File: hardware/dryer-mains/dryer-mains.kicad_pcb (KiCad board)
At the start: 2 copper layers, 64 x 85 mm, 19 parts, among them K1 SRD-05VDC-SL-C, K2 SRD-05VDC-SL-C, Q1 MMBT2222A, Q2 MMBT2222A

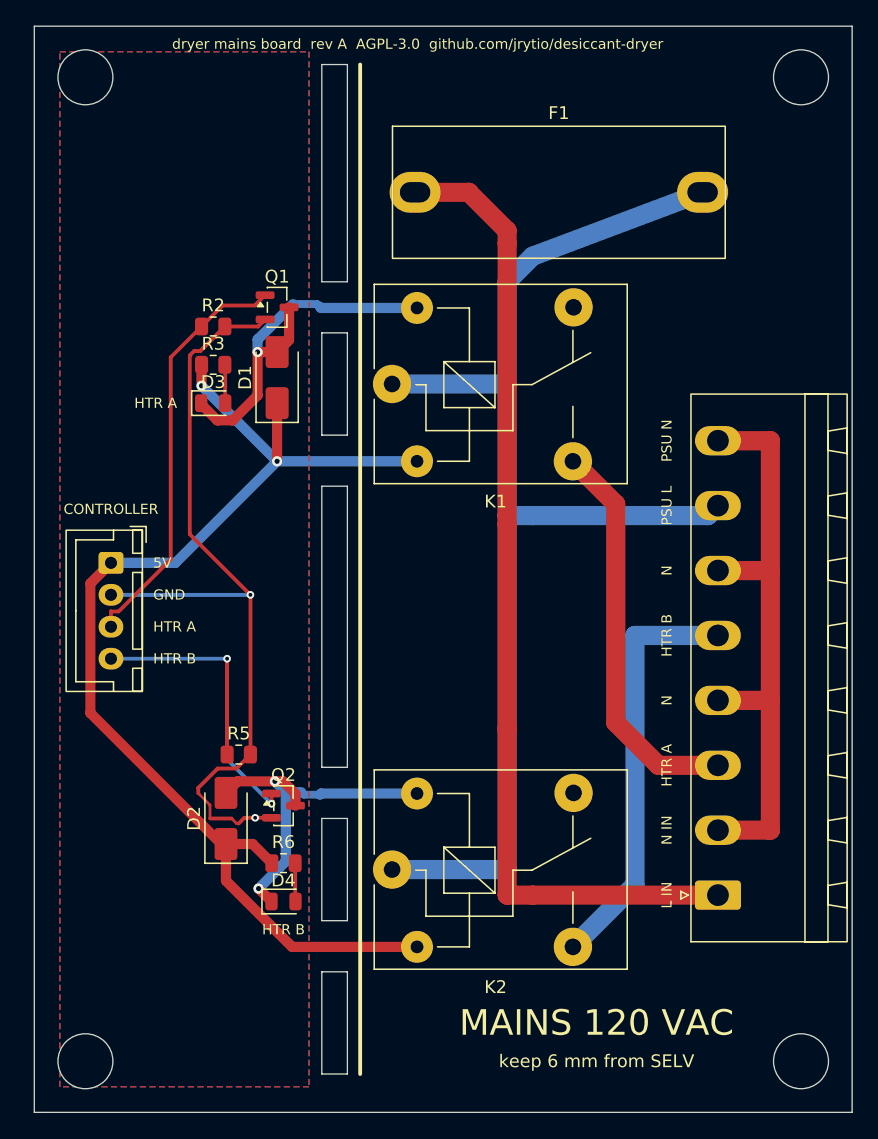
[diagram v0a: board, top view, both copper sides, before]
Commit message: Fit the controller and mains boards to 85 x 70 and 45 x 70 mm
The reviewer's enclosure spaces are 85 x 70 mm (controller) and 45 x 70 mm
(mains); the split boards were 76 x 85 and 64 x 85. New tests pin the
outlines before DRC: each board's declared size and Edge.Cuts geometry,
the corner holes 4 mm in, every courtyard inside the outline (the ESP
sockets, J_MAINS and the M4 head courtyards excepted), no hole under the
Thing Plus body, and the same link pinout on J_RLY and J_CTRL.

Controller: the Thing Plus lies along the long edge, USB-C face 3 mm past
the left edge, antenna keep-out at the right end starting past the last
socket pads (a no-pads keep-out cannot cover them). J_RLY and J_SENS on
the right edge clear of the M4 courtyards; J_24V, J_DISP (along the edge)
and J_LOADS at the bottom; the 5 V block, 24 V chain and MOSFET stages in
between. Silk re-pointed; the title moves to the back, and the edge
connectors' references are hidden behind their pin legends.

Mains: SELV strip x 0-7 in two columns, slot x 7-9 with gaps at the coil
pads, relays with COM at x 12, F1 across the top at y 14 (the J_MAINS
courtyard and H2's fix it there), J_MAINS pads at x 39.5 with N linked on
the plug side. MAINS_TRACKS re-laid with the rev A arrangement and
distances (measured): 6.27 mm to SELV outside the relay areas, 3.5 inside,
1.8 mm L to L, 1.1 mm L to N, 7.8 mm from F1 to H2's hole edge. The GND
pour starts at y 21 so its outline, not a rules-aware refill, keeps F1
6.7 mm from it: board.build fills before the project's rules exist. The
relay-area spine tests in test_project follow the new spine and areas.

Both boards regenerated fresh and unrouted; DRC shows only unconnected
items. test_routed_board's DRC-clean and fully-routed checks fail until
the boards are routed (next task).

Co-Authored-By: Claude Opus 5.5 <noreply@anthropic.com>
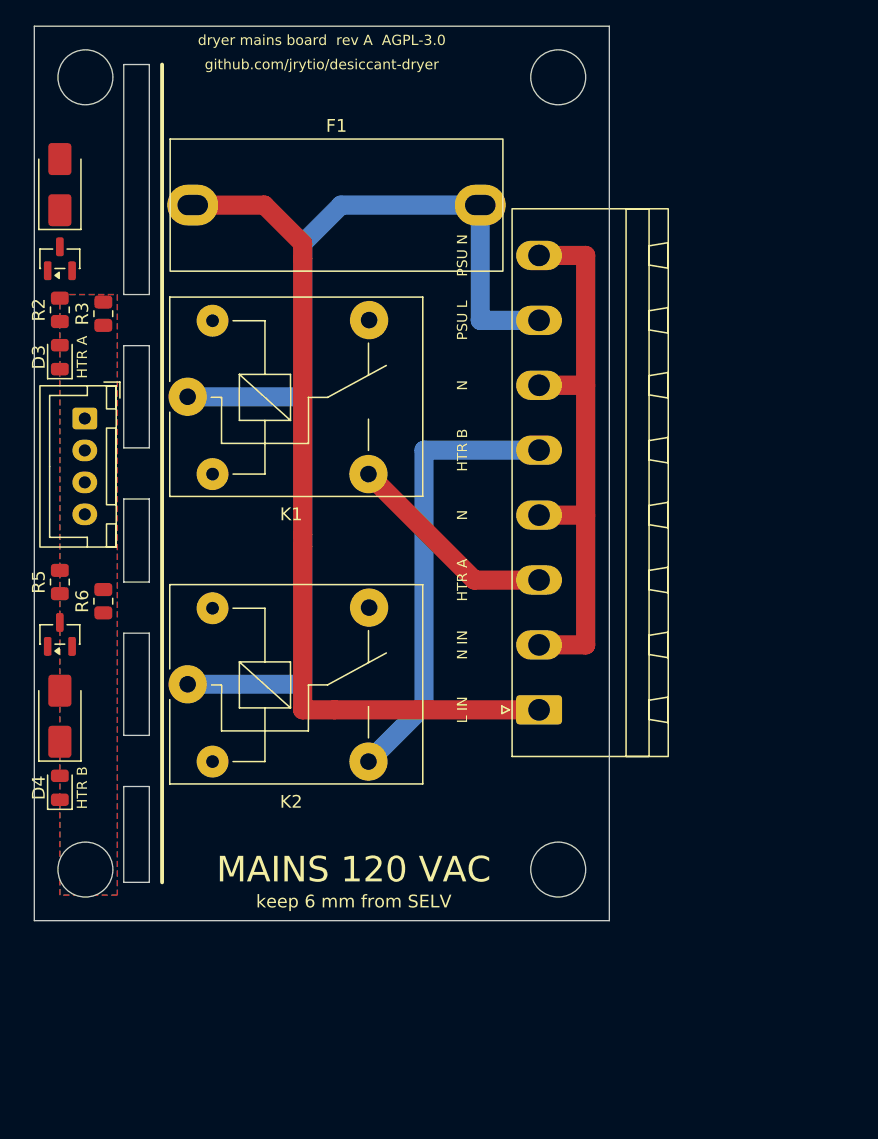
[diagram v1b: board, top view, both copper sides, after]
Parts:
- moved R6 24.9 mm to (5.40, 45.0), turned to 90 degrees
- moved H4 24.2 mm to (41.0, 66.0)
- moved D1 22.7 mm to (2.00, 12.4)
- moved Q2 22.0 mm to (2.00, 47.6), turned to 90 degrees
- moved K2 21.6 mm to (12.0, 51.5)
- moved J_MAINS 20.2 mm to (39.5, 53.5)
- moved D4 19.6 mm to (2.00, 59.6), turned to 90 degrees
- moved R5 19.4 mm to (2.00, 43.5), turned to 90 degrees
- moved H2 19.0 mm to (41.0, 4.00)
- moved F1 17.4 mm to (12.4, 14.0)
- moved Q1 17.4 mm to (2.00, 18.2), turned to 90 degrees
- moved K1 16.0 mm to (12.0, 29.0)
- moved D2 15.3 mm to (2.00, 54.0)
- moved H3 15.0 mm to (4.00, 66.0)
- moved D3 12.5 mm to (2.00, 25.9), turned to 90 degrees
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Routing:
- net +5V: track 93.2 -> 0.00 mm, vias 2 -> 0
- net GND: track 64.3 -> 0.00 mm, vias 2 -> 0
- net RLY_A: track 32.8 -> 0.00 mm
- net RLY_B: track 30.2 -> 0.00 mm, vias 2 -> 0
- net COIL_A: track 29.4 -> 0.00 mm, vias 1 -> 0
- net COIL_B: track 28.6 -> 0.00 mm, vias 2 -> 0
- net L_FUSED: track 97.9 -> 81.3 mm
- net L_SW_A: track 31.2 -> 16.8 mm
- net L_IN: track 76.9 -> 64.8 mm
- net LED_HA_R: track 3.01 -> 0.00 mm
- net LED_HB_R: track 3.01 -> 0.00 mm
- net L_SW_B: track 32.9 -> 35.2 mm
- net N: track 46.9 -> 45.1 mm
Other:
- board size 64 x 85 mm -> 45 x 70 mm
- board text added: "5V GND HTR A HTR B"
- board text added: "dryer mains board rev A AGPL-3.0"
- board text added: "github.com/jrytio/desiccant-dryer"
- board text removed: "5V"
- board text removed: "GND"
- board text removed: "dryer mains board rev A AGPL-3.0 github.com/jrytio/desiccant-dryer"

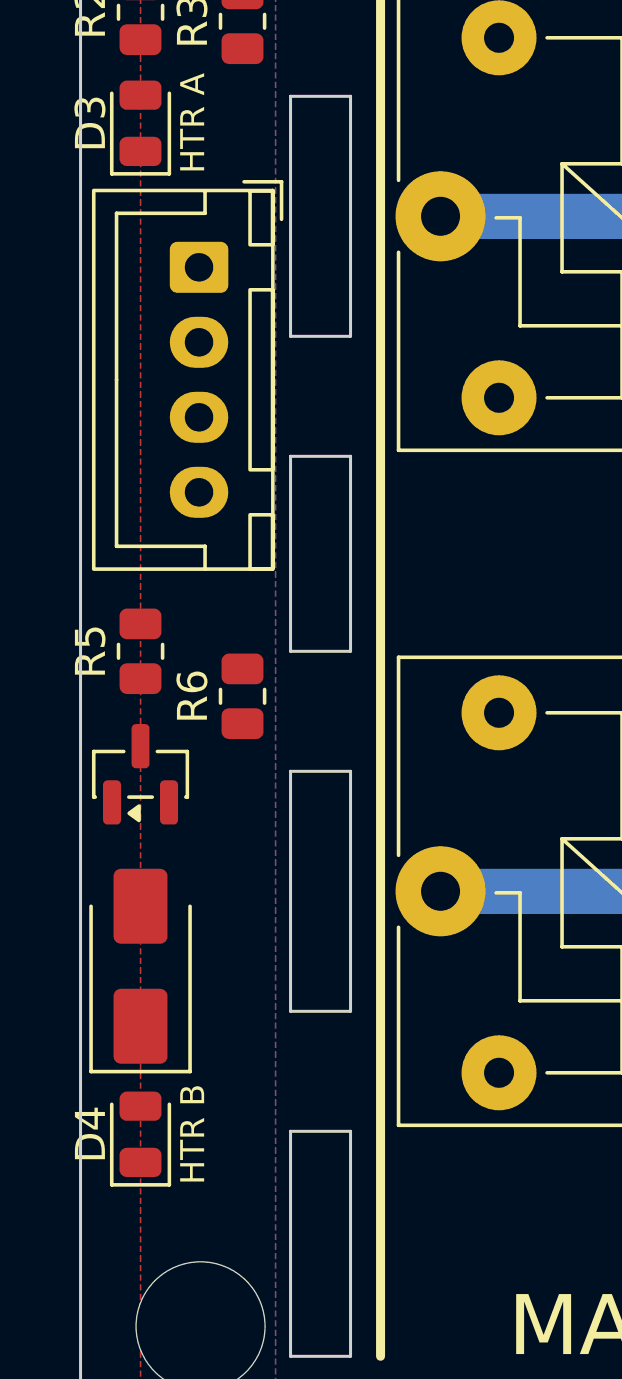
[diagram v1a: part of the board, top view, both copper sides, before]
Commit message: Keep the link header 6 mm from the relay COM pads and bound the plug overhang
Review of the 45 x 70 mains board: J_CTRL's +5V pin sat 5.67 mm from K1's
COM, passing only on the relay-area 3.5 mm relaxation, which exists for
the relay's own coil-to-COM geometry. J_CTRL moves down to pins y 33-40.5
(6.32 mm from K1's COM, 11.21 from K2's) and driver B is re-stacked down
the edge column below it, with only R6 in the second column, so every
strip pad keeps the plain 6 mm from both COM pads.

test_courtyards_inside no longer exempts J_MAINS and the ESP sockets
outright: J_MAINS may leave the mains board's right edge by at most
5.1 mm and nowhere else, and the sockets must lie inside (the Thing Plus
body overhangs, not its socket footprints).

Comments: L to N is 1.10 mm against the 1.0 rule (1.55 on the single
board; regaining it would put F1's pad 1 at the slot's 1 mm limit); the
pour clears F1's pad by 7.34 mm, its outline corner 6.66 mm from the
pad's bounding box; F1's pad edge is 1.4 mm from the slot.

Co-Authored-By: Claude Opus 5.5 <noreply@anthropic.com>
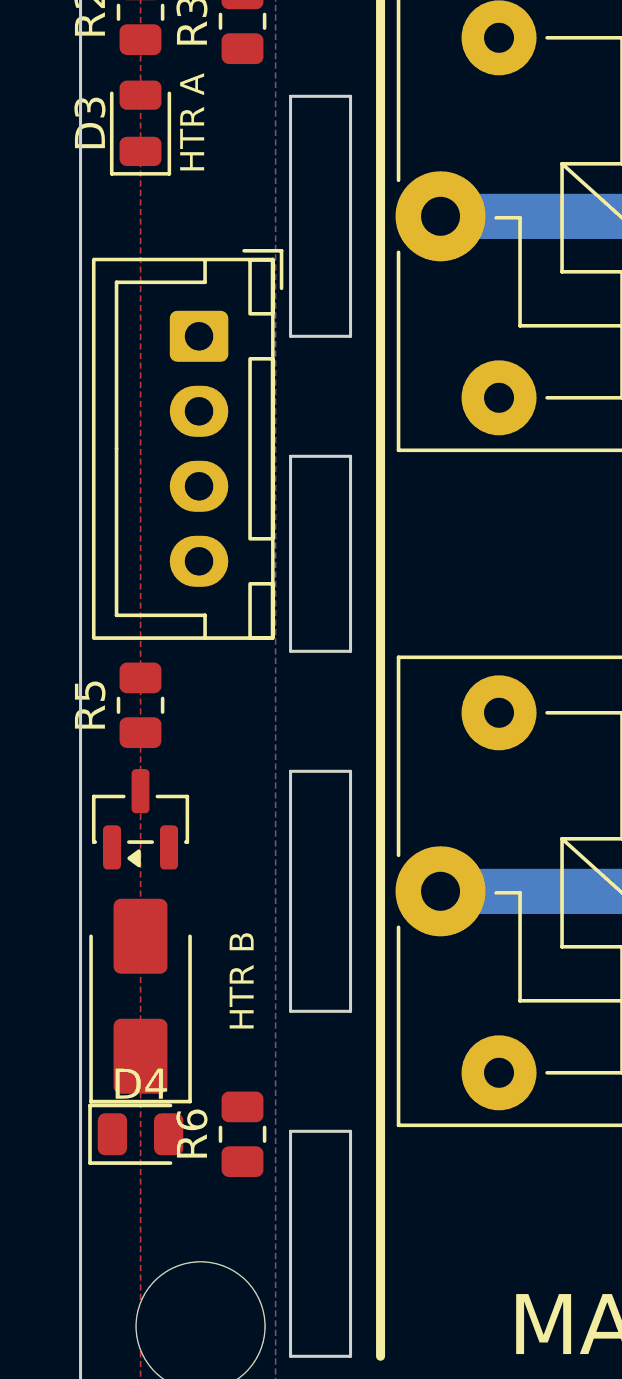
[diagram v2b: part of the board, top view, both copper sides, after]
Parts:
- moved R6 14.6 mm to (5.40, 59.6)
- moved J_CTRL 2.30 mm to (3.95, 33.0)
- moved R5 1.80 mm to (2.00, 45.3)
- moved Q2 1.50 mm to (2.00, 49.1)
- moved D2 1.00 mm to (2.00, 55.0)
- turned D4 to 0 degrees
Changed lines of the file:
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@@
 	(footprint "LED_SMD:LED_0805_2012Metric"
 		(layer "F.Cu")
-		(at 2 59.6 90)
+		(at 2 59.6)
 		(descr "LED SMD 0805 (2012 Metric), square (rectangular) end terminal, IPC-7351 nominal, (Body size source: https://docs.google.com/spreadsheets/d/1BsfQQcO9C6DZCsRaXUlFlo91Tg2WpOkGARC1WS5S8t0/edit?usp=sharing)")
 		(tags "LED")
 		(property "Reference" "D4"
-			(at 0 -1.65 90)
+			(at 0 -1.65 0)
 			(layer "F.SilkS")
 			(effects
@@
 		)
 		(property "Value" "LED red"
-			(at 0 1.65 90)
+			(at 0 1.65 0)
 			(layer "F.Fab")
 			(effects
@@
 		)
 		(property "Datasheet" ""
-			(at 0 0 90)
+			(at 0 0 0)
 			(layer "F.Fab")
 			(hide yes)
@@
 		)
 		(property "Description" ""
-			(at 0 0 90)
+			(at 0 0 0)
 			(layer "F.Fab")
 			(hide yes)
@@
 		)
 		(property "KiLib_Generator" "SMD_2terminal_chip_molded"
-			(at 0 0 90)
+			(at 0 0 0)
 			(layer "F.SilkS")
 			(hide yes)
@@
 		(duplicate_pad_numbers_are_jumpers no)
 		(fp_line
-			(start 1 -0.96)
-			(end -1.685 -0.96)
+			(start -1.685 -0.96)
+			(end -1.685 0.96)
 			(stroke
 				(width 0.12)
@@
 		)
 		(fp_line
-			(start -1.685 -0.96)
-			(end -1.685 0.96)
+			(start -1.685 0.96)
+			(end 1 0.96)
 			(stroke
 				(width 0.12)
@@
 		)
 		(fp_line
-			(start -1.685 0.96)
-			(end 1 0.96)
+			(start 1 -0.96)
+			(end -1.685 -0.96)
 			(stroke
 				(width 0.12)
@@
 		)
 		(fp_line
-			(start 1 -0.6)
-			(end -0.7 -0.6)
+			(start -1 -0.3)
+			(end -1 0.6)
 			(stroke
 				(width 0.1)
@@
 		)
 		(fp_line
-			(start -0.7 -0.6)
-			(end -1 -0.3)
+			(start -1 0.6)
+			(end 1 0.6)
 			(stroke
 				(width 0.1)
@@
 		)
 		(fp_line
-			(start -1 -0.3)
-			(end -1 0.6)
+			(start -0.7 -0.6)
+			(end -1 -0.3)
 			(stroke
 				(width 0.1)
@@
 		)
 		(fp_line
-			(start 1 0.6)
-			(end 1 -0.6)
+			(start 1 -0.6)
+			(end -0.7 -0.6)
 			(stroke
 				(width 0.1)
@@
 		)
 		(fp_line
-			(start -1 0.6)
-			(end 1 0.6)
+			(start 1 0.6)
+			(end 1 -0.6)
 			(stroke
 				(width 0.1)
@@
 		)
 		(fp_text user "${REFERENCE}"
-			(at 0 0 90)
+			(at 0 0 0)
 			(layer "F.Fab")
 			(effects
@@
 		)
 		(pad "1" smd roundrect
-			(at -0.9375 0 90)
+			(at -0.9375 0)
 			(size 0.975 1.4)
 			(layers "F.Cu" "F.Mask" "F.Paste")
@@
 		)
 		(pad "2" smd roundrect
-			(at 0.9375 0 90)
+			(at 0.9375 0)
 			(size 0.975 1.4)
 			(layers "F.Cu" "F.Mask" "F.Paste")
@@
 	(footprint "Package_TO_SOT_SMD:SOT-23"
 		(layer "F.Cu")
-		(at 2 47.6 90)
+		(at 2 49.1 90)
 		(descr "SOT, 3 Pin (JEDEC TO-236 Var AB https://www.jedec.org/document_search?search_api_views_fulltext=TO-236)")
 		(tags "SOT TO_SOT_SMD")
@@
 	(footprint "Diode_SMD:D_SMA"
 		(layer "F.Cu")
-		(at 2 54 90)
+		(at 2 55 90)
 		(descr "Diode SMA (DO-214AC)")
 		(tags "Diode SMA (DO-214AC)")
@@
 	(footprint "Resistor_SMD:R_0805_2012Metric"
 		(layer "F.Cu")
-		(at 5.4 45 90)
+		(at 5.4 59.6 90)
 		(descr "Resistor SMD 0805 (2012 Metric), square (rectangular) end terminal, IPC-7351 nominal, (Body size source: IPC-SM-782 page 72, https://www.pcb-3d.com/wordpress/wp-content/uploads/ipc-sm-782a_amendment_1_and_2.pdf)")
 		(tags "resistor")
@@
 	(footprint "Resistor_SMD:R_0805_2012Metric"
 		(layer "F.Cu")
-		(at 2 43.5 90)
+		(at 2 45.3 90)
 		(descr "Resistor SMD 0805 (2012 Metric), square (rectangular) end terminal, IPC-7351 nominal, (Body size source: IPC-SM-782 page 72, https://www.pcb-3d.com/wordpress/wp-content/uploads/ipc-sm-782a_amendment_1_and_2.pdf)")
 		(tags "resistor")
@@
 	(footprint "Connector_JST:JST_XH_B4B-XH-A_1x04_P2.50mm_Vertical"
 		(layer "F.Cu")
-		(at 3.95 30.7 -90)
+		(at 3.95 33 -90)
 		(descr "JST XH series connector, B4B-XH-A (http://www.jst-mfg.com/product/pdf/eng/eXH.pdf)")
 		(tags "connector JST XH vertical")
@@
 	)
 	(gr_text "HTR B"
-		(at 3.75 59.6 90)
+		(at 5.4 54.5 90)
 		(layer "F.SilkS")
 		(effects
@@
 	)
 	(gr_text "5V  GND  HTR A  HTR B"
-		(at 1.05 34.45 90)
+		(at 1.05 36.75 90)
 		(layer "B.SilkS")
 		(effects
@@
 	)
 	(gr_text "CONTROLLER"
-		(at 6 34.45 90)
+		(at 6 36.75 90)
 		(layer "B.SilkS")
 		(effects

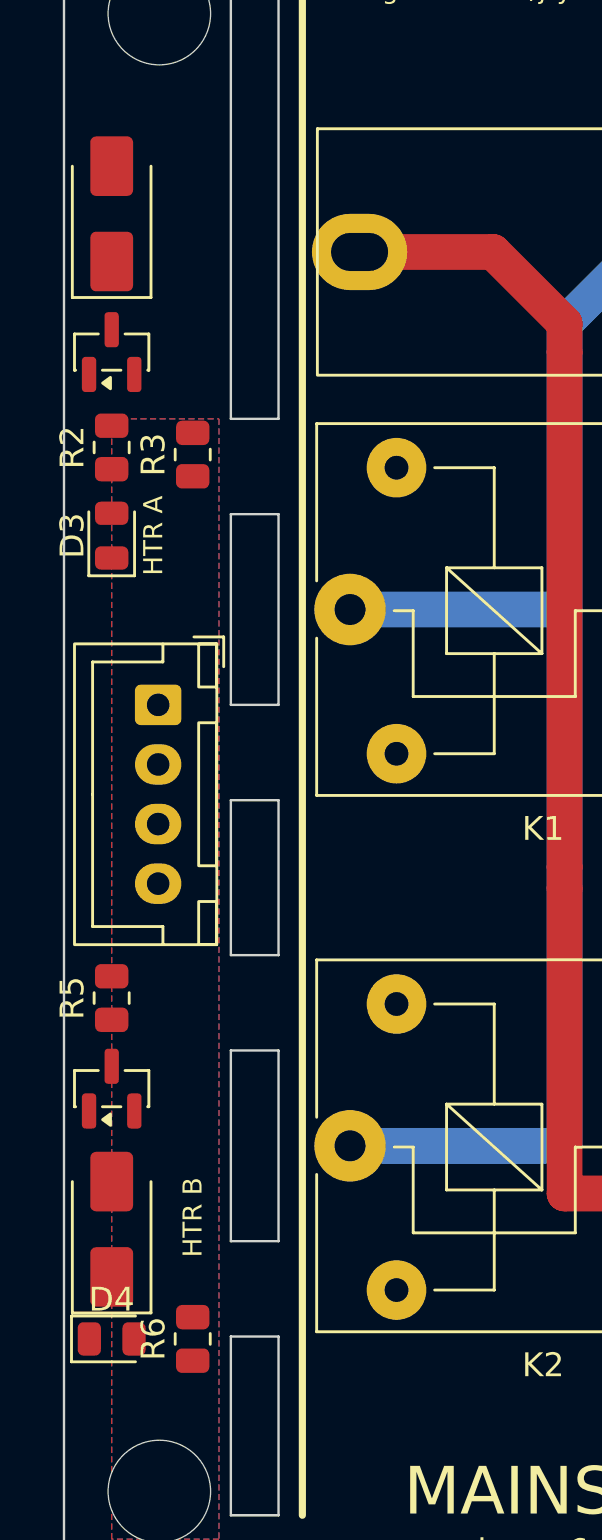
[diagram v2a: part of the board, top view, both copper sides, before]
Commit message: Route both boards at their enclosure sizes
Both boards are routed with Freerouting 2.5.0 (200 passes) and are DRC
clean with every pad connected: controller 477 tracks, mains 171.

The router copy now carries what the router could not see:
- a 0.55 mm keep-out band inside the outline, since Freerouting keeps
  only its 0.2 mm clearance from the edge and the project needs 0.5;
- a keep-out round each mains pad or track outside the relay areas,
  grown by 5.85 mm (6.05 with the router's own clearance), so SELV
  routes in the strip keep the 6 mm "mains to selv" rule beside F1's
  pad 1 (6.07 mm measured, COIL_A).
After the import, a track the optimiser necked below the project's
0.2 mm minimum (two 0.18 mm LCD_RST pieces, with room for 0.3) goes
back to its netclass width; DRC judges the result.

The saved pour fill now honours the project rules: board.build and
route.route refill and save through kicad-cli (drc --refill-zones
--save-board) once the .kicad_pro and .kicad_dru are on disk, then
put the canonical .kicad_pro back. Before, the pcbnew filler ran with
only the zone's own 0.3 mm clearance, so DRC's refill could pass while
the copper the gerbers are plotted from sat closer to mains. The gerber
and SVG exports pass --check-zones. Two tests: the committed mains
board's GND fill keeps 6 mm from mains copper outside the relay areas
and 3.5 inside, and a scratch mains board with the pour drawn 3.9 mm
from F1's pad 1 comes out of board.build pulled back (it fails with
the refill disabled).

Co-Authored-By: Claude Opus 5.5 <noreply@anthropic.com>
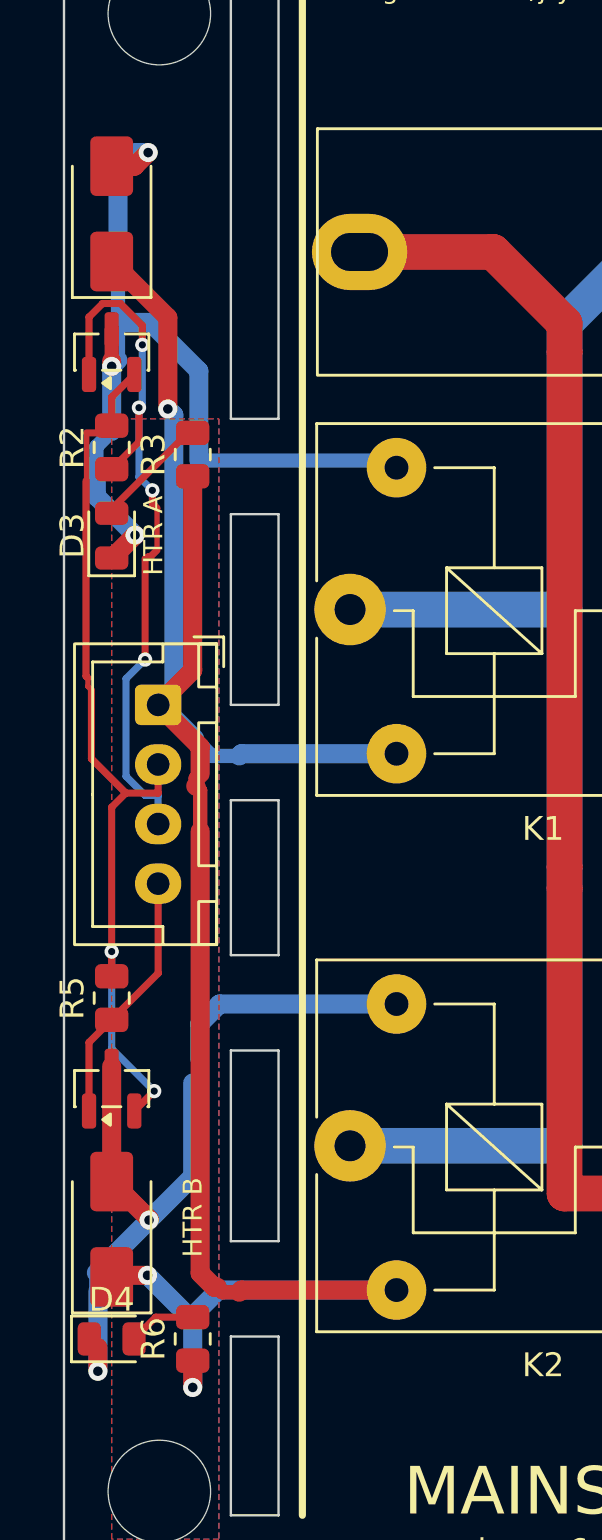
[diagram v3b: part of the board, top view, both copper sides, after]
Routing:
- net +5V: track 0.00 -> 91.7 mm, vias 0 -> 3
- net COIL_A: track 0.00 -> 39.4 mm, vias 0 -> 3
- net GND: track 0.00 -> 37.8 mm, vias 0 -> 2
- net COIL_B: track 0.00 -> 33.6 mm, vias 0 -> 2
- net RLY_A: track 0.00 -> 31.1 mm, vias 0 -> 4
- net RLY_B: track 0.00 -> 10.7 mm
- net LED_HA_R: track 0.00 -> 4.90 mm
- net LED_HB_R: track 0.00 -> 2.84 mm
